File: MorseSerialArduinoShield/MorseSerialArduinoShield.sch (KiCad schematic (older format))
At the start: 12 parts, among them U1 SC39-11SRWA

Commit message: done design
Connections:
- net at R8.2: now also A1.26 (D11); no longer A1.22 (D7)
- net at A1.20 (D5): now also R7.2; no longer R6.2
- net at A1.21 (D6): now also R6.2; no longer R7.2
- net at A1.23 (D8): now also R2.2; no longer R3.2
- net at A1.25 (D10): now also R3.2; no longer R2.2
- net at R1.2: now also A1.22 (D7); no longer A1.26 (D11)
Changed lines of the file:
@@
 	4050 2450 4050 2800
-Wire Wire Line
-	4050 2450 4400 2450
 Wire Wire Line
 	5650 1550 6400 1550
@@
 	6400 1550 6400 2600
 Connection ~ 5650 1550
-Wire Wire Line
-	4950 2100 4950 1900
-Wire Wire Line
-	4950 1900 5300 1900
-Wire Wire Line
-	4300 2100 4950 2100
-Wire Wire Line
-	5300 2200 5300 2100
-Wire Wire Line
-	3650 2200 5300 2200
-Wire Wire Line
-	5150 2700 5150 3300
-Wire Wire Line
-	5150 3300 5300 3300
 Wire Wire Line
 	4150 2700 5150 2700
@@
 	5300 2300 5300 2350
 Wire Wire Line
-	4650 1900 4650 1700
-Wire Wire Line
-	4650 1700 5300 1700
-Wire Wire Line
-	3650 1900 4650 1900
-Wire Wire Line
 	5300 2500 5300 2600
 Wire Wire Line
 	4200 2500 5300 2500
 Wire Wire Line
-	4700 2000 4700 2800
+	4050 2450 4400 2450
 Wire Wire Line
-	4700 2800 5300 2800
+	4250 2400 4250 2800
 Wire Wire Line
-	4250 3050 5300 3050
+	4250 2800 5300 2800
 Wire Wire Line
-	4250 2400 4250 3050
+	4700 2000 4700 3050
+Wire Wire Line
+	4700 3050 5300 3050
+Wire Wire Line
+	3650 2200 5100 2200
+Wire Wire Line
+	3650 1900 4850 1900
+Wire Wire Line
+	5150 2700 5150 1700
+Wire Wire Line
+	5150 1700 5300 1700
+Wire Wire Line
+	5100 2200 5100 1900
+Wire Wire Line
+	5100 1900 5300 1900
+Wire Wire Line
+	4300 2100 5300 2100
+Wire Wire Line
+	4850 3300 5300 3300
+Wire Wire Line
+	4850 1900 4850 3300
 $EndSCHEMATC

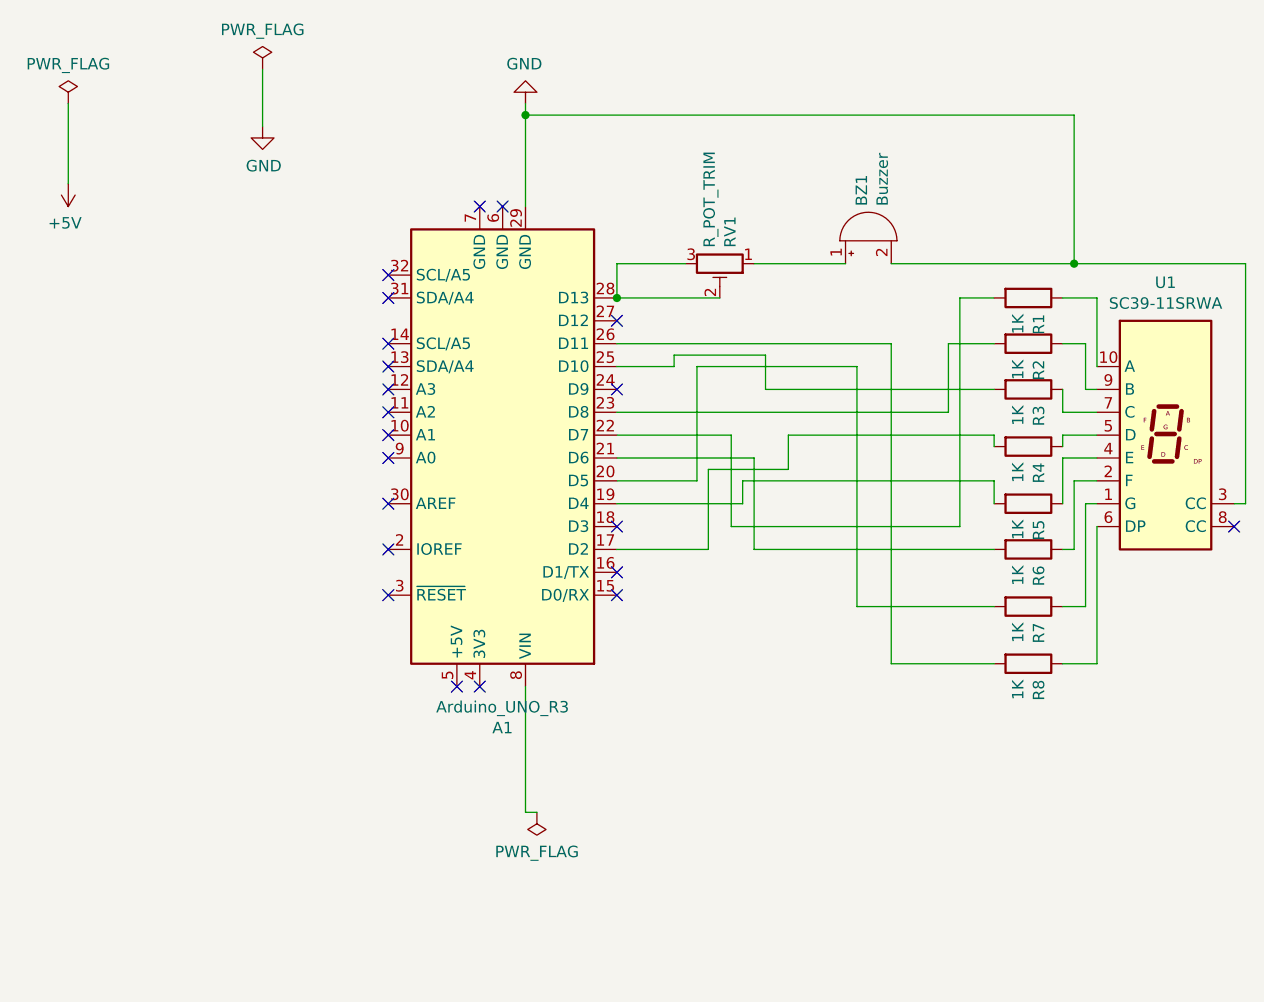
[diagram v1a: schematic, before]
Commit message: Untested Bluetooth variant using HC-05
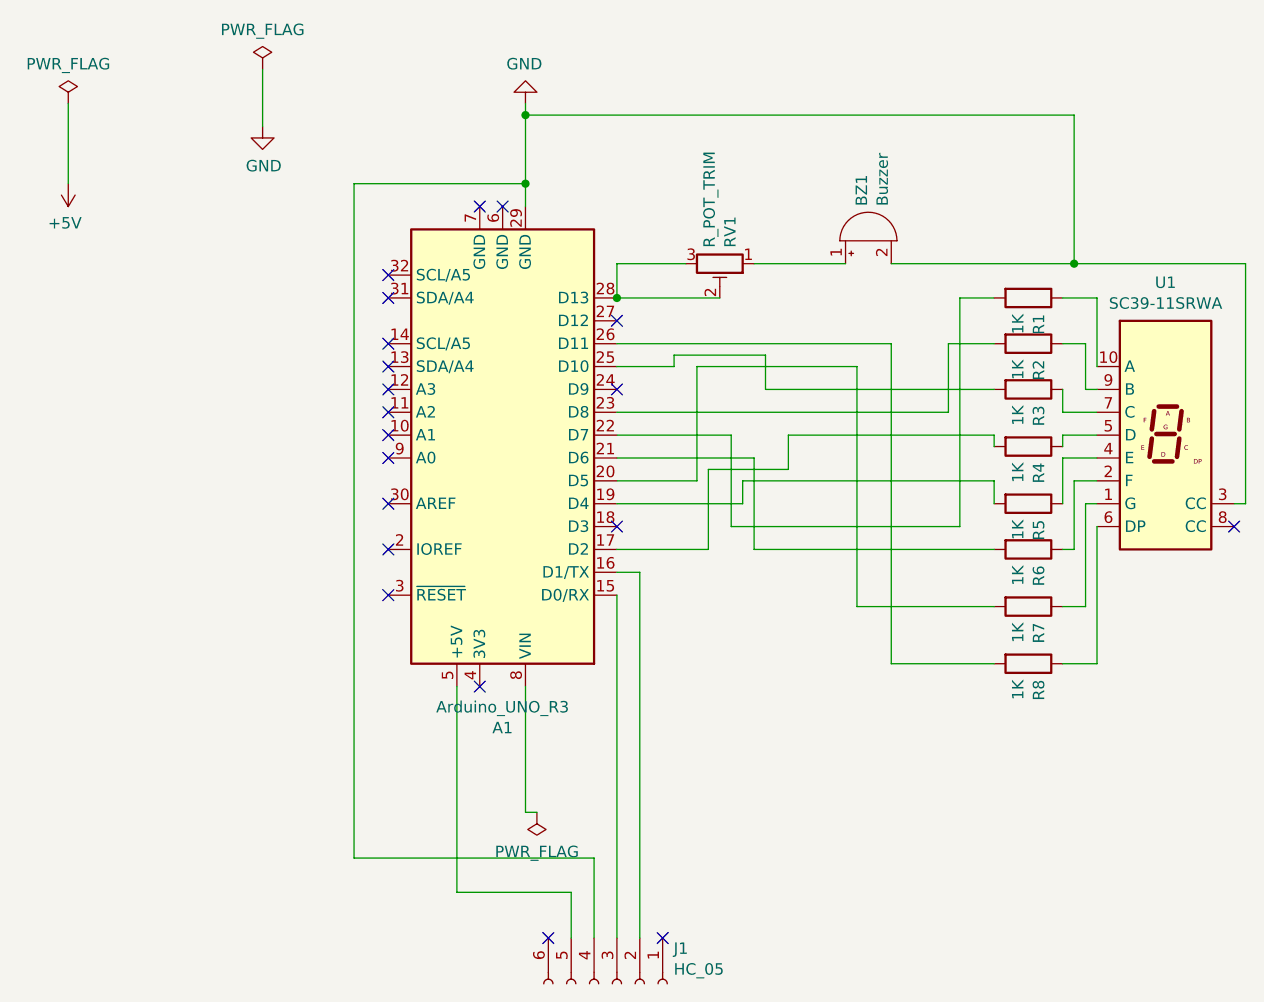
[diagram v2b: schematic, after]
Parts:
- added J1: HC_05, Connector_PinSocket_2.54mm:PinSocket_1x06_P2.54mm_Vertical, symbol Connector:Conn_01x06_Female
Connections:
- net GND: now also J1.4 (Pin_4)
- net at A1.15 (D0/RX): now also J1.3 (Pin_3)
- net at A1.16 (D1/TX): now also J1.2 (Pin_2)
- net at A1.5 (+5V): now also J1.5 (Pin_5)
- no-connect marks 21 -> 20
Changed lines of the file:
@@
 	6400 2600 6350 2600
 NoConn ~ 6350 2700
-NoConn ~ 3650 3000
-NoConn ~ 3650 2900
 NoConn ~ 3650 2700
 NoConn ~ 3650 2100
 NoConn ~ 3650 1800
 NoConn ~ 3050 3400
-NoConn ~ 2950 3400
 NoConn ~ 2650 3000
 NoConn ~ 2650 2800
@@
 NoConn ~ 2650 1600
 Wire Wire Line
-	3250 900  3250 1300
+	3250 900  3250 1200
 $Comp
 L power:PWR_FLAG #FLG0101
@@
 Wire Wire Line
 	4850 1900 4850 3300
+$Comp
+L Connector:Conn_01x06_Female J1
+U 1 1 61A275DC
+P 3650 4700
+F 0 "J1" V 3496 4948 50  0000 L CNN
+F 1 "HC_05" V 3587 4948 50  0000 L CNN
+F 2 "Connector_PinSocket_2.54mm:PinSocket_1x06_P2.54mm_Vertical" H 3650 4700 50  0001 C CNN
+F 3 "~" H 3650 4700 50  0001 C CNN
+	1    3650 4700
+	0    1    1    0
+$EndComp
+NoConn ~ 3350 4500
+Wire Wire Line
+	2950 3400 2950 4300
+Wire Wire Line
+	2950 4300 3450 4300
+Wire Wire Line
+	3450 4300 3450 4500
+Wire Wire Line
+	3550 4500 3550 4150
+Wire Wire Line
+	3550 4150 2500 4150
+Wire Wire Line
+	2500 4150 2500 1200
+Wire Wire Line
+	2500 1200 3250 1200
+Connection ~ 3250 1200
+Wire Wire Line
+	3250 1200 3250 1300
+Wire Wire Line
+	3650 4500 3650 3000
+Wire Wire Line
+	3750 4500 3750 2900
+Wire Wire Line
+	3750 2900 3650 2900
+NoConn ~ 3850 4500
 $EndSCHEMATC

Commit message: Added external power pins for a battery and added JLC marker for production when ready
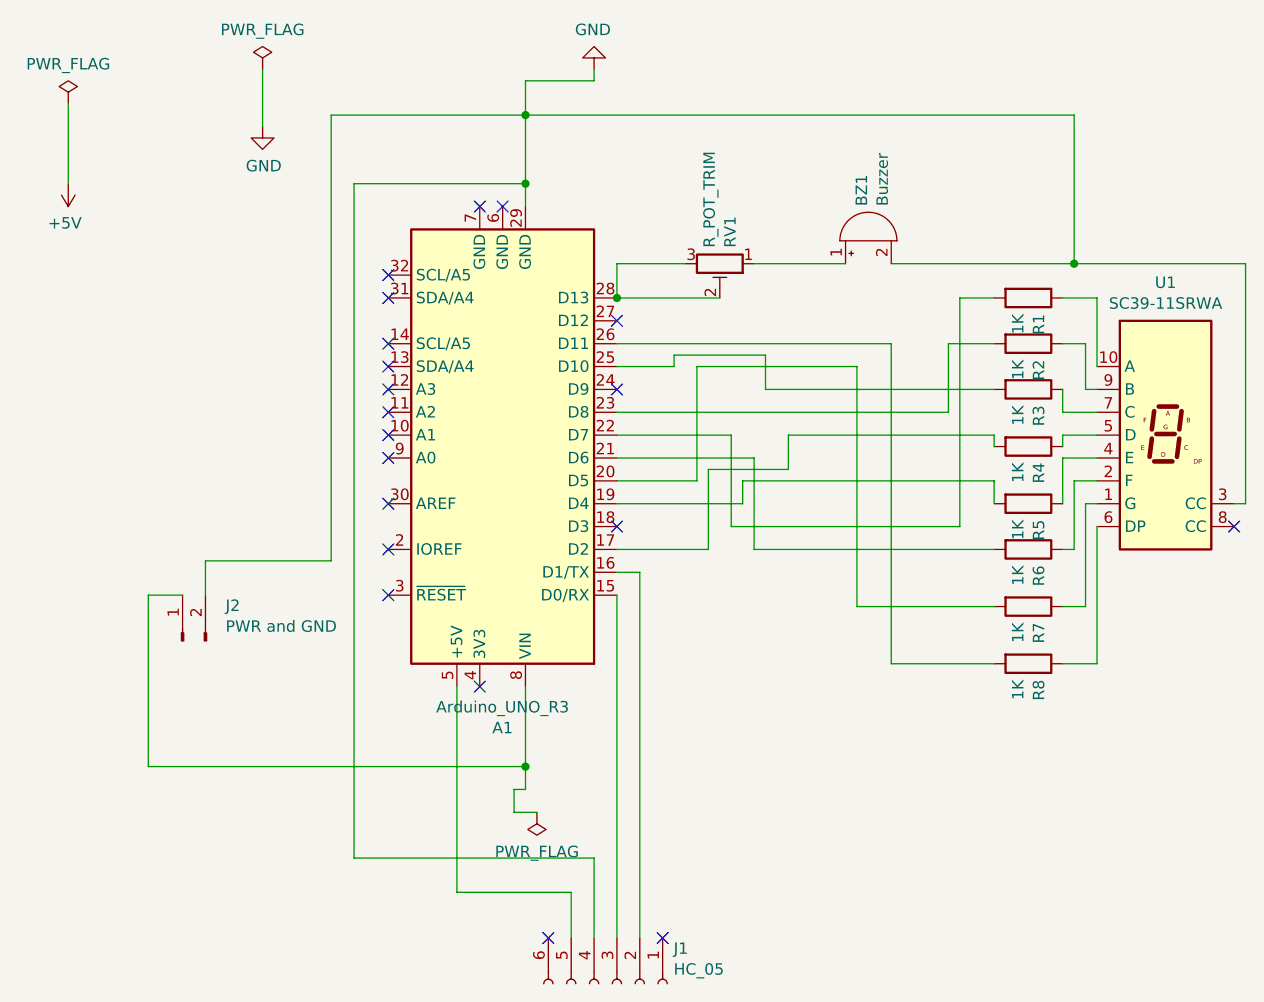
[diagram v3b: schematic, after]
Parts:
- added J2: PWR and GND, Connector_PinSocket_2.54mm:PinSocket_1x02_P2.54mm_Vertical, symbol Connector:Conn_01x02_Male
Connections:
- net GND: now also J2.2 (Pin_2)
- net at A1.8 (VIN): now also J2.1 (Pin_1)
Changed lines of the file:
@@
 	-1   0    0    1
 $EndComp
-Wire Wire Line
-	3250 3400 3250 3950
-Wire Wire Line
-	3250 3950 3300 3950
 NoConn ~ 3150 1300
 NoConn ~ 3050 1300
@@
 L power:GND #PWR0103
 U 1 1 5EE0BAD3
-P 3250 850
-F 0 "#PWR0103" H 3250 600 50  0001 C CNN
-F 1 "GND" H 3255 677 50  0000 C CNN
-F 2 "" H 3250 850 50  0001 C CNN
-F 3 "" H 3250 850 50  0001 C CNN
-	1    3250 850
+P 3550 700
+F 0 "#PWR0103" H 3550 450 50  0001 C CNN
+F 1 "GND" H 3555 527 50  0000 C CNN
+F 2 "" H 3550 700 50  0001 C CNN
+F 3 "" H 3550 700 50  0001 C CNN
+	1    3550 700
 	-1   0    0    1
 $EndComp
-Wire Wire Line
-	3250 850  3250 900
 Connection ~ 3250 900
 Wire Wire Line
@@
 	3750 2900 3650 2900
 NoConn ~ 3850 4500
+Wire Wire Line
+	3250 750  3550 750
+Wire Wire Line
+	3550 750  3550 700
+Wire Wire Line
+	3250 3850 3200 3850
+Wire Wire Line
+	3200 3950 3300 3950
+$Comp
+L Connector:Conn_01x02_Male J2
+U 1 1 61A52F04
+P 1750 3200
+F 0 "J2" V 1904 3012 50  0000 R CNN
+F 1 "PWR and GND" V 1813 3012 50  0000 R CNN
+F 2 "Connector_PinSocket_2.54mm:PinSocket_1x02_P2.54mm_Vertical" H 1750 3200 50  0001 C CNN
+F 3 "~" H 1750 3200 50  0001 C CNN
+	1    1750 3200
+	0    -1   -1   0
+$EndComp
+Wire Wire Line
+	3250 750  3250 900
+Wire Wire Line
+	3200 3850 3200 3950
+Wire Wire Line
+	3250 3400 3250 3750
+Wire Wire Line
+	3250 3750 1600 3750
+Wire Wire Line
+	1600 3750 1600 3000
+Wire Wire Line
+	1600 3000 1750 3000
+Connection ~ 3250 3750
+Wire Wire Line
+	3250 3750 3250 3850
+Wire Wire Line
+	3250 900  2400 900
+Wire Wire Line
+	2400 900  2400 2850
+Wire Wire Line
+	2400 2850 1850 2850
+Wire Wire Line
+	1850 2850 1850 3000
 $EndSCHEMATC
